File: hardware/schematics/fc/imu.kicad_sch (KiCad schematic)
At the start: 3 parts, among them U6 LSM6DSV16XTR

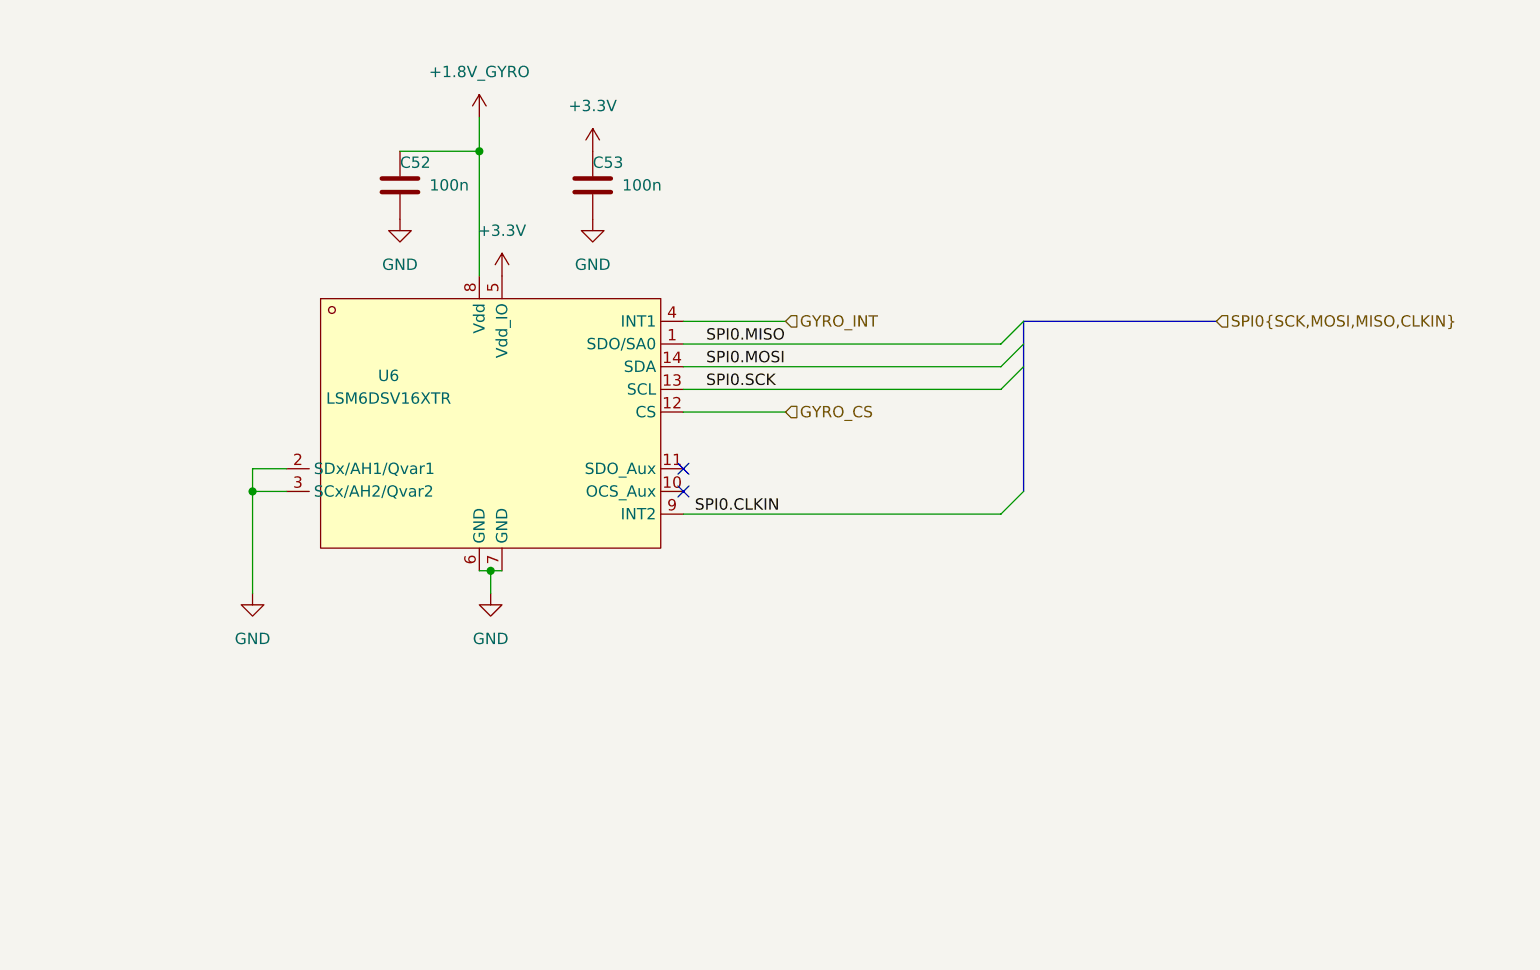
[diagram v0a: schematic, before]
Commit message: Whoop setup: restructure, import current FC/RX sheets, Bluejay libs, research docs
- KiCad project moved under hardware/ (family convention)
- FC sheets <- OpenFC-Lite-Mini rev2 (osd dropped: digital-only, root never
  referenced it); ELRS sheet <- OpenRX-Lite; orphaned esc_main deleted;
  esc_channel x4 kept as inherited placeholder pending Bluejay redraw
- Libraries replaced: lib (Lite-Mini), components/4in1ESC (4in1-mini donors),
  OpenRX-Shared (3D paths rewritten project-local via pcbnew API), new 'whoop'
  lib re-imported fresh via easyeda2kicad (EFM8BB51F16G, AGM310MAP, BY25Q64)
- sym-lib-table duplicate stale iCloud OpenRX-Shared entries fixed
- datasheets/ assembled (FC/ESC/ELRS); stale toothpick ESC docs removed
- docs/ESC_DESIGN.md extended with 2026-06 sourcing + market reality check
  (AGM310MAP thermal/supply limits, 12A class floor, BY25Q64 substitute)
- README/market research rewritten for digital-only Bluejay whoop scope
- Hierarchy verified via kicad-cli netlist export

Co-Authored-By: Claude Fable 5 <noreply@anthropic.com>
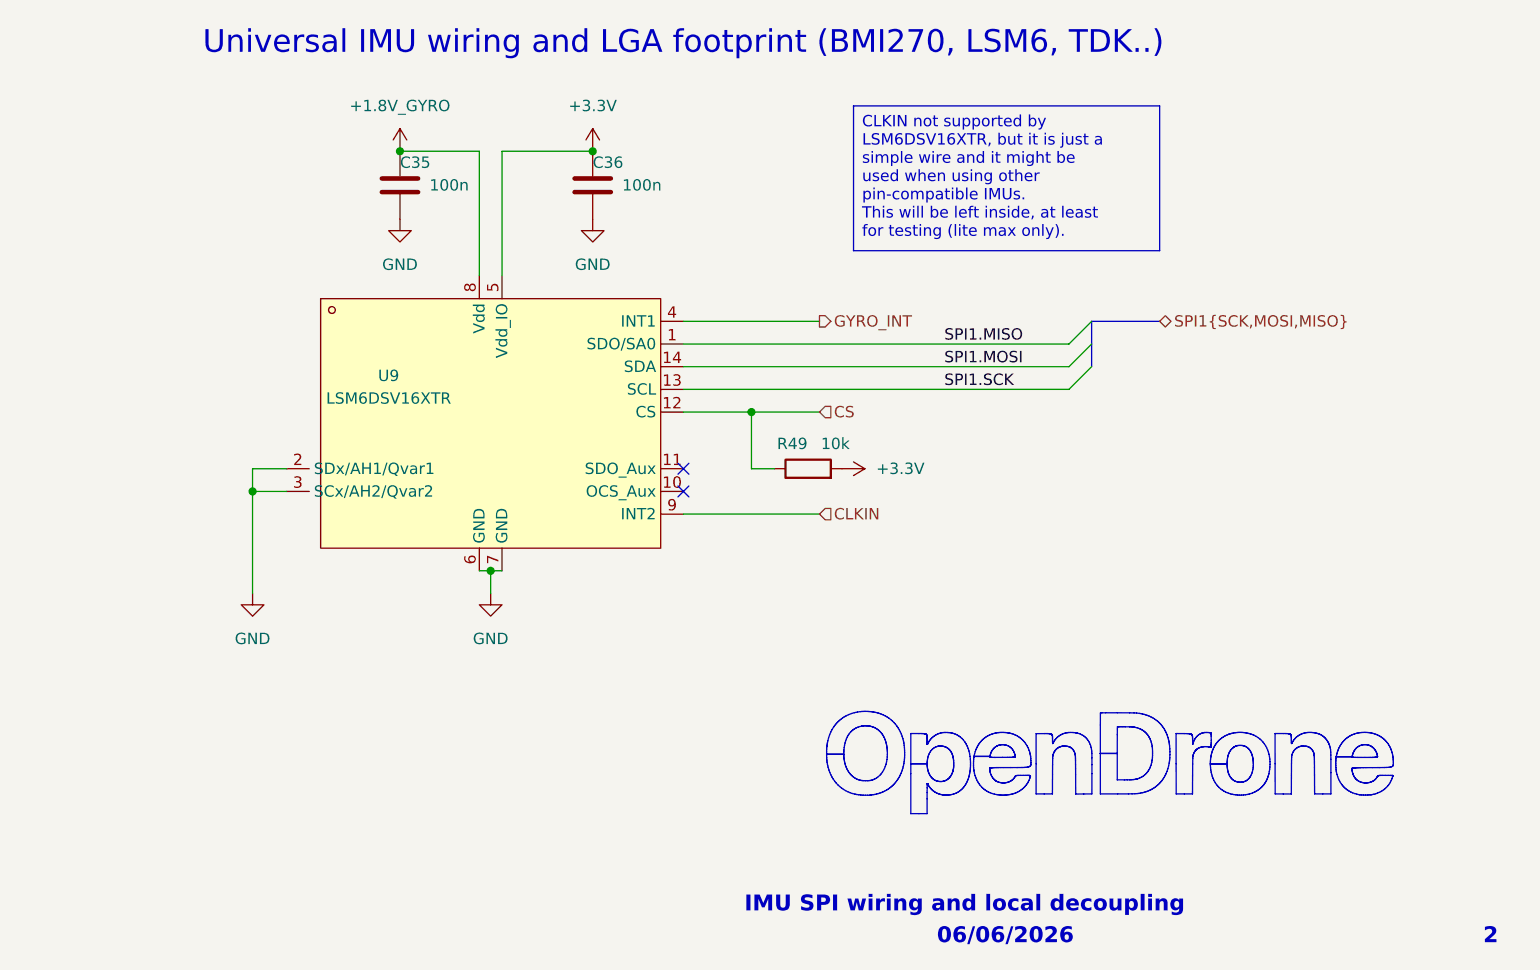
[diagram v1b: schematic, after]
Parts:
- added R49: 10k, Resistor_SMD:R_0201_0603Metric, symbol Device:R
- U9: renamed from U6; LCSC (none) -> C5267406; LCSC Part C5267406 -> (none)
- renumbered C52 to C35, C53 to C36
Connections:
- net +3.3V: now also R49.2
- net GYRO_CS renamed CS
- net CS: now also R49.1
- net SPI0.CLKIN renamed CLKIN
- net SPI0.MISO renamed SPI1.MISO
- net SPI0.MOSI renamed SPI1.MOSI
- net SPI0.SCK renamed SPI1.SCK
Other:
- note added: "06/06/2026"
- note added: "2"
- note added: "IMU SPI wiring and local decoupling"
- note added: "Universal IMU wiring and LGA footprint (BMI270, LSM6, TDK..)"
